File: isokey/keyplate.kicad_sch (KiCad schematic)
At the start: 166 parts

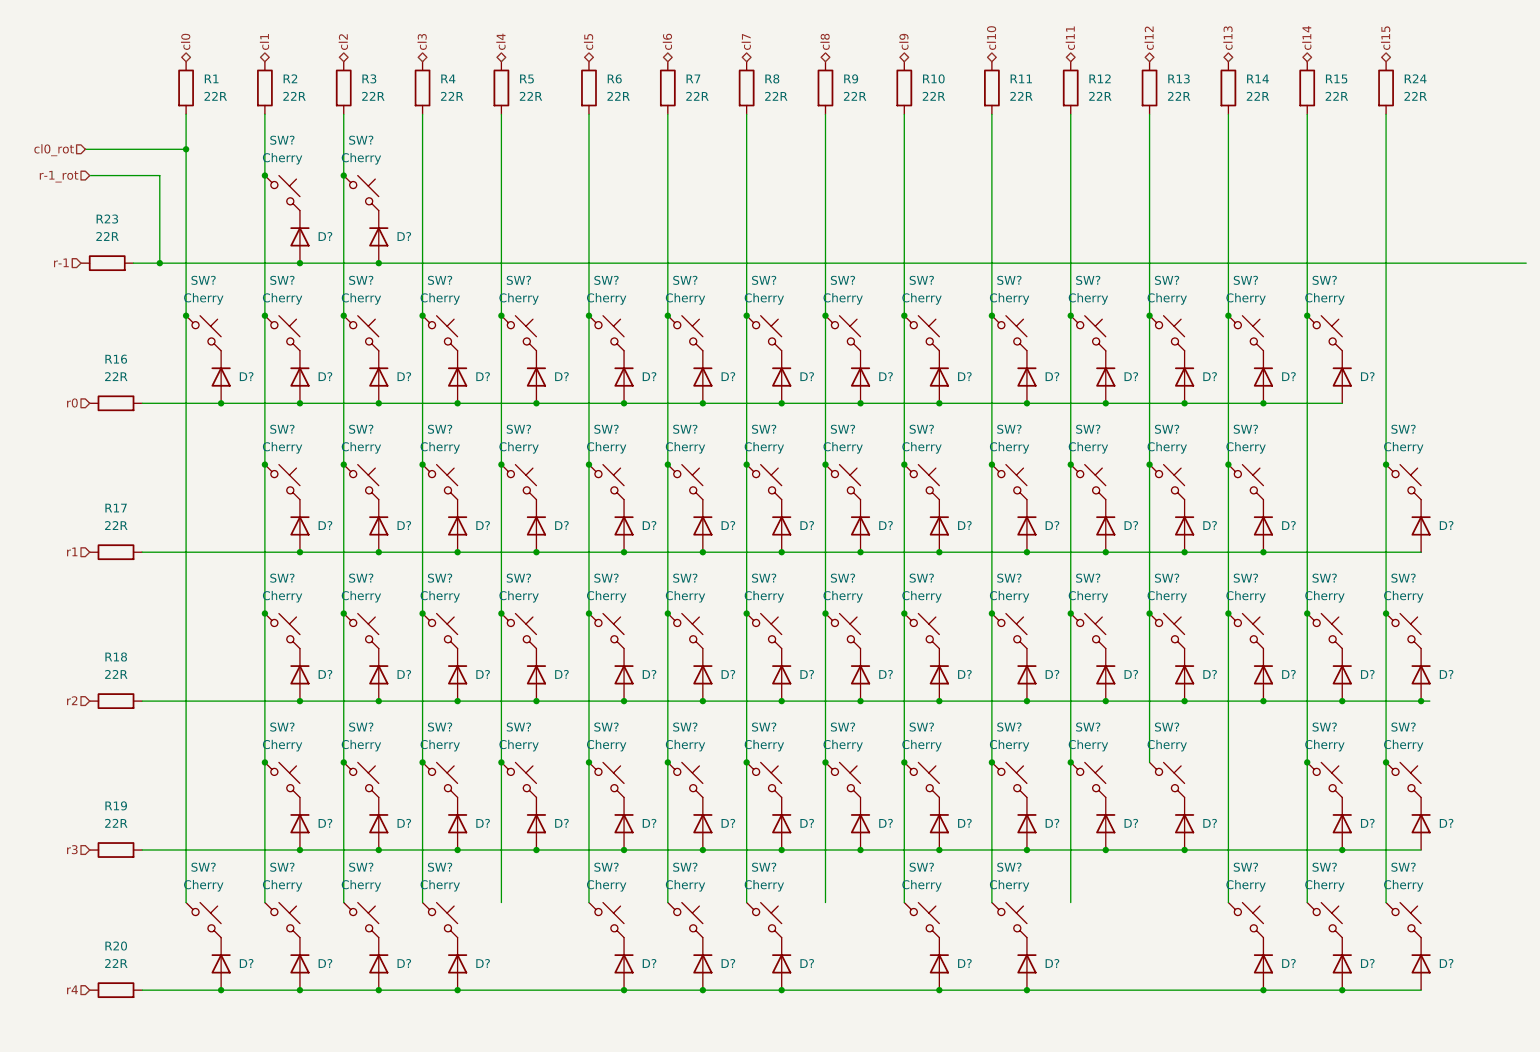
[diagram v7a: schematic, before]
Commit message: Update scheme. Continue routing.
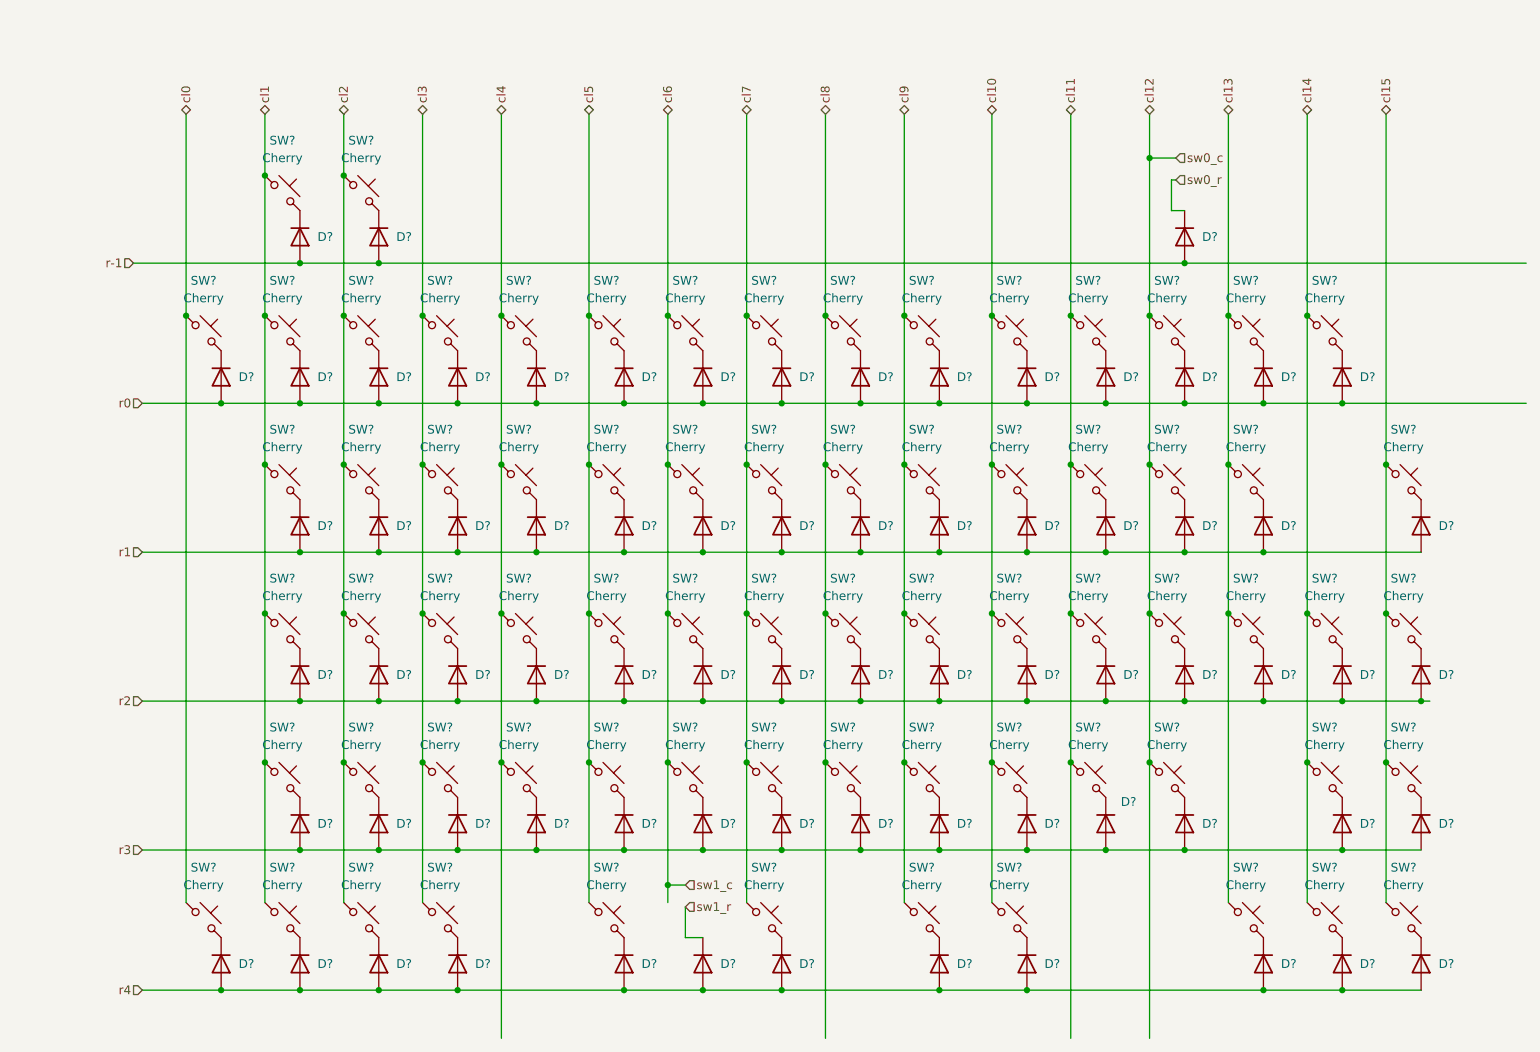
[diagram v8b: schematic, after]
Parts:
- removed R1, R10, R11, R12, R13, R14, R15, R16, R17, R18, R19, R2, R20, R23, R24, R3, R4, R5, R6, R7, R8, R9: 22R, Resistor_SMD:R_0603_1608Metric_Pad0.98x0.95mm_HandSolder, symbol Device:R
- removed SW?: Cherry, Button_Switch_Keyboard:Kailh_socket_MX_LED, symbol Switch:SW_Push_45deg
- added D?: 1N4448W, Diode_SMD:D_SOD-123, symbol Diode:1N4448W
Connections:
- net cl0_rot is gone; now on net cl0: SW?.1, SW?.1
- net r-1_rot is gone; now on net r-1: D?.2 (A), D?.2 (A)
- net cl1: now also SW?.1, SW?.1, SW?.1, SW?.1, SW?.1, SW?.1
- net cl10: now also SW?.1, SW?.1, SW?.1, SW?.1, SW?.1
- net cl11: now also SW?.1, SW?.1, SW?.1, SW?.1
- net cl12: now also SW?.1, SW?.1, SW?.1, SW?.1
- net cl13: now also SW?.1, SW?.1, SW?.1, SW?.1
- net cl14: now also SW?.1, SW?.1, SW?.1, SW?.1
- net cl15: now also SW?.1, SW?.1, SW?.1, SW?.1
- net cl2: now also SW?.1, SW?.1, SW?.1, SW?.1, SW?.1, SW?.1
- net cl3: now also SW?.1, SW?.1, SW?.1, SW?.1, SW?.1
- net cl4: now also SW?.1, SW?.1, SW?.1, SW?.1
- net cl5: now also SW?.1, SW?.1, SW?.1, SW?.1, SW?.1
- net cl6: now also SW?.1, SW?.1, SW?.1, SW?.1
- net cl7: now also SW?.1, SW?.1, SW?.1, SW?.1, SW?.1
- net cl8: now also SW?.1, SW?.1, SW?.1, SW?.1
- net cl9: now also SW?.1, SW?.1, SW?.1, SW?.1, SW?.1
- net r-1: now also D?.2 (A)
- net r0: now also D?.2 (A), D?.2 (A), D?.2 (A), D?.2 (A), D?.2 (A), D?.2 (A), D?.2 (A), D?.2 (A), D?.2 (A), D?.2 (A), D?.2 (A), D?.2 (A), D?.2 (A), D?.2 (A), D?.2 (A)
- net r1: now also D?.2 (A), D?.2 (A), D?.2 (A), D?.2 (A), D?.2 (A), D?.2 (A), D?.2 (A), D?.2 (A), D?.2 (A), D?.2 (A), D?.2 (A), D?.2 (A), D?.2 (A), D?.2 (A)
- net r2: now also D?.2 (A), D?.2 (A), D?.2 (A), D?.2 (A), D?.2 (A), D?.2 (A), D?.2 (A), D?.2 (A), D?.2 (A), D?.2 (A), D?.2 (A), D?.2 (A), D?.2 (A), D?.2 (A), D?.2 (A)
- net r3: now also D?.2 (A), D?.2 (A), D?.2 (A), D?.2 (A), D?.2 (A), D?.2 (A), D?.2 (A), D?.2 (A), D?.2 (A), D?.2 (A), D?.2 (A), D?.2 (A), D?.2 (A), D?.2 (A)
- net r4: now also D?.2 (A), D?.2 (A), D?.2 (A), D?.2 (A), D?.2 (A), D?.2 (A), D?.2 (A), D?.2 (A), D?.2 (A), D?.2 (A), D?.2 (A), D?.2 (A)
- net sw1_r: now reaches D?.1 (K)
- new net sw0_r: D?.1 (K)
